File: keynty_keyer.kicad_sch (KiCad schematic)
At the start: 43 parts, among them SW1 Power

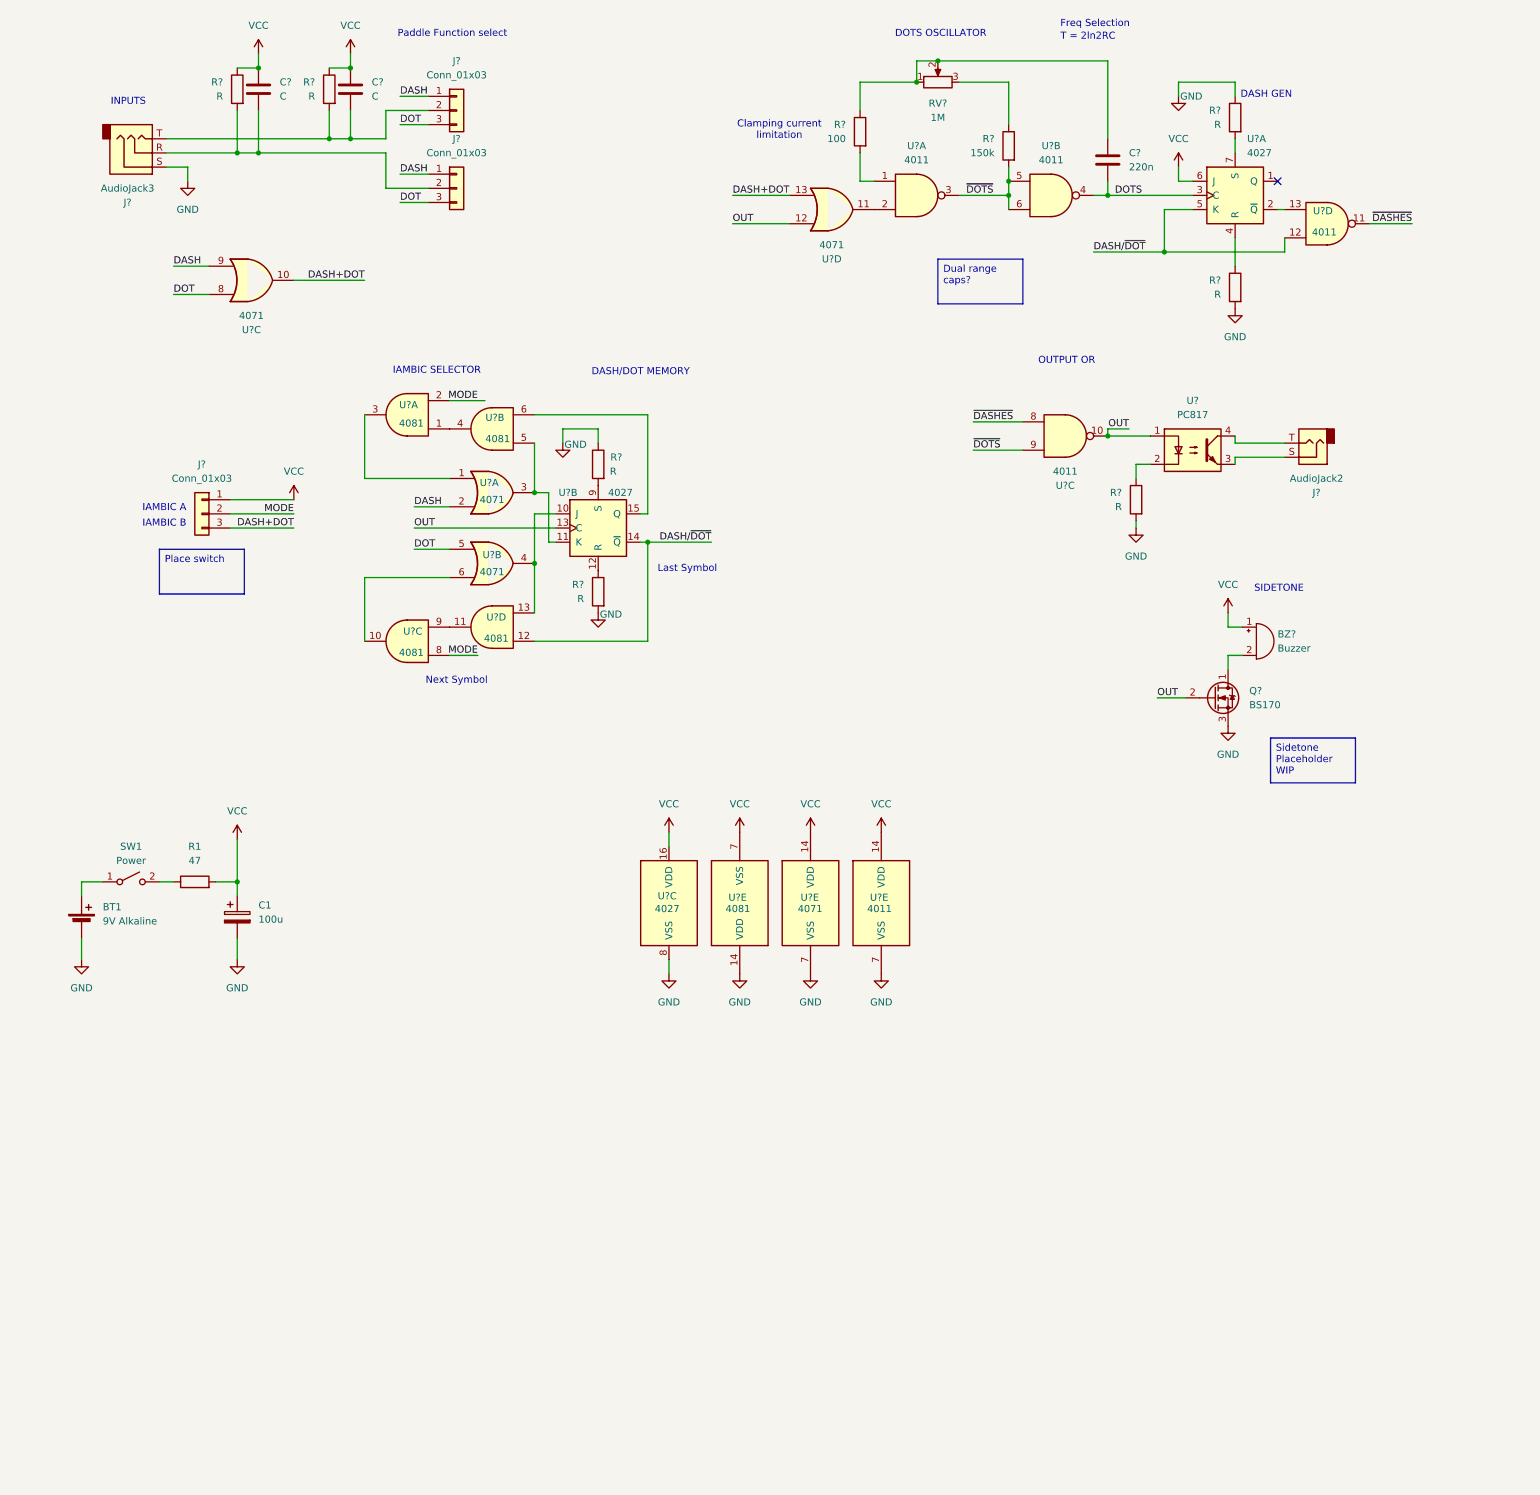
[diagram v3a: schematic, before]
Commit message: added matteo sidetononi e matteo powerleddoni
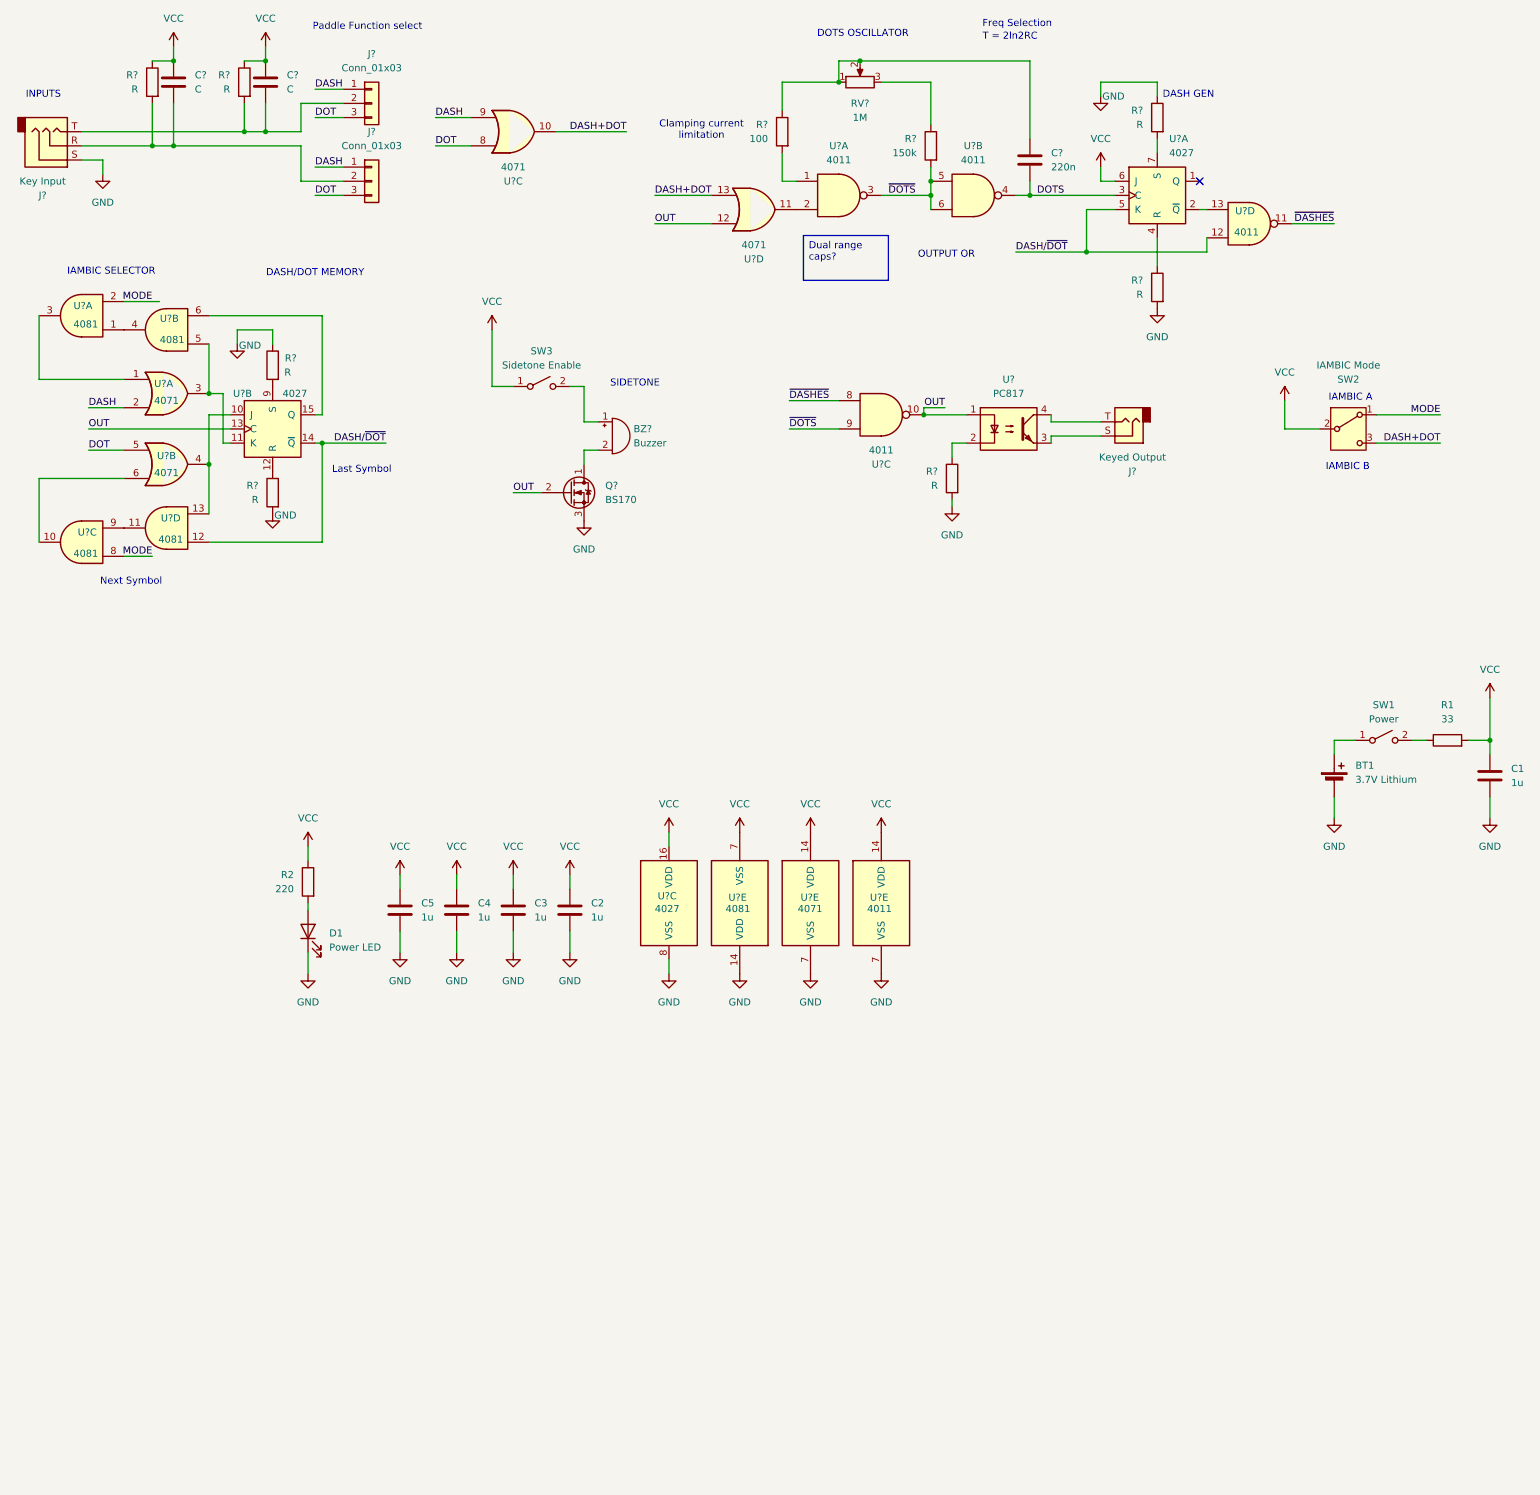
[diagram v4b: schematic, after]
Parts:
- removed C1: 100u, symbol Device:C_Polarized
- removed J?: Conn_01x03, symbol Connector_Generic:Conn_01x03
- added C1, C2, C3, C4, C5: 1u, symbol Device:C
- added D1: Power LED, symbol Device:LED
- added R2: 220, symbol Device:R
- added SW2: IAMBIC Mode, symbol Switch:SW_SPDT
- added SW3: Sidetone Enable, symbol Switch:SW_SPST
- BT1: value 9V Alkaline -> 3.7V Lithium
- J?: value AudioJack3 -> Key Input
- J?: value AudioJack2 -> Keyed Output
- R1: value 47 -> 33
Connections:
- net DASH+DOT: now also SW2.3 (C)
- net GND: now also C1.2, C2.2, C3.2, C4.2, C5.2, D1.1 (K)
- net MODE: now also SW2.1 (A)
- net VCC: now also C1.1, C2.1, C3.1, C4.1, C5.1, R2.1, SW2.2 (B), SW3.1 (A); no longer BZ?.1 (+)
- new net: D1.2 (A), R2.2
- new net: BZ?.1 (+), SW3.2 (B)
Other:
- moved on the sheet: BT1, BZ?, C?, J?, Q?, R1, R?, RV?, SW1, U?, U?A, U?B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

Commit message: corrected IAMBIC selector,added footprints, first PCB Draft
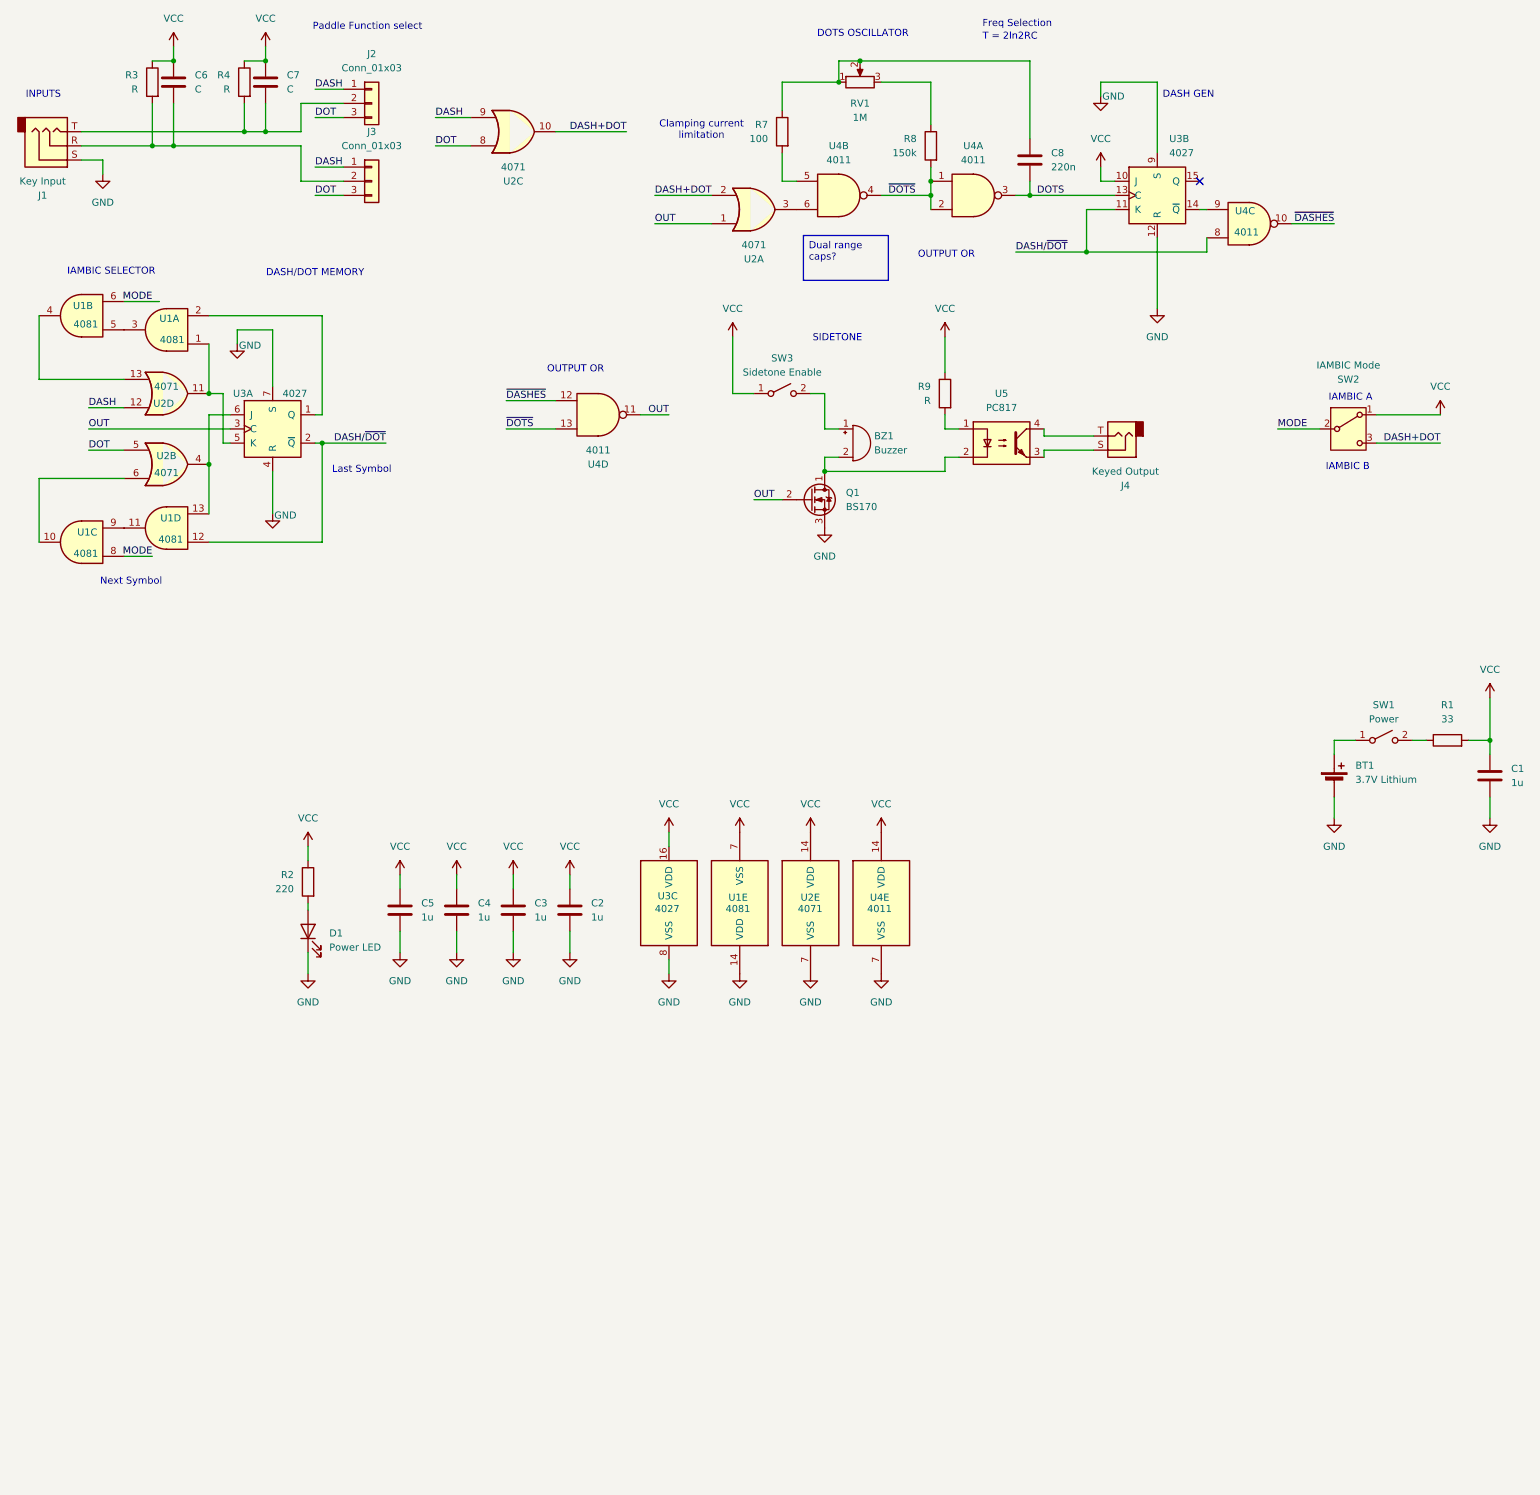
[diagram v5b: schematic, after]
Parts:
- removed R? (x4): R, symbol Device:R
- BT1: footprint (none) -> Battery:BatteryHolder_Keystone_2462_2xAA
- BZ1: renamed from BZ?; footprint (none) -> Buzzer_Beeper:Buzzer_12x9.5RM7.6
- C1, C2, C3, C4, C5: footprint (none) -> Capacitor_SMD:C_0805_2012Metric
- C6, C7, C8: renamed from C?; footprint (none) -> Capacitor_SMD:C_0603_1608Metric
- D1: footprint (none) -> LED_SMD:LED_0603_1608Metric
- J1, J4: renamed from J?; footprint (none) -> Connector_Audio:Jack_3.5mm_CUI_SJ1-3513N_Horizontal
- J2, J3: renamed from J?; footprint (none) -> Connector_PinHeader_2.54mm:PinHeader_1x03_P2.54mm_Vertical
- Q1: renamed from Q?; footprint Package_TO_SOT_THT:TO-92_Inline -> Package_TO_SOT_SMD:SOT-23-3
- R1, R2: footprint (none) -> Resistor_SMD:R_0603_1608Metric
- R3, R4, R7, R8, R9: renamed from R?; footprint (none) -> Resistor_SMD:R_0603_1608Metric
- RV1: renamed from RV?; footprint (none) -> Potentiometer_THT:Potentiometer_Alps_RK09K_Single_Vertical
- SW1, SW2, SW3: footprint (none) -> Button_Switch_THT:SW_Slide_SPDT_Straight_CK_OS102011MS2Q
- U1, U2, U4: renamed from U?; footprint (none) -> Package_SO:SOIC-14_3.9x8.7mm_P1.27mm
- U3: renamed from U?; footprint (none) -> Package_SO:SOIC-16_3.9x9.9mm_P1.27mm
- U5: renamed from U?; footprint Package_DIP:DIP-4_W7.62mm_LongPads -> Package_DIP:DIP-4_W8.89mm_SMDSocket_LongPads
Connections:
- net DASH: now also U2.12; no longer U2.2
- net DASH+DOT: now also U2.2; no longer U2.13
- net DASH/~{DOT}: now also U3.11 (K), U3.2 (~{Q}), U4.8; no longer U3.14 (~{Q}), U3.5 (K), U4.12
- net DOTS: now also U3.13 (C), U4.3; no longer U3.3 (C), U4.4
- net GND: now also U3.12 (R), U3.4 (R), U3.7 (S), U3.9 (S); no longer R9.2
- net MODE: now also SW2.2 (B), U1.6; no longer SW2.1 (A), U1.2
- net OUT: now also U2.1, U3.3 (C), U4.11; no longer U2.12, U3.13 (C), U4.10, U5.1
- net VCC: now also R9.1, SW2.1 (A), U3.10 (J); no longer SW2.2 (B), U3.6 (J)
- net ~{DASHES}: now also U4.10, U4.12; no longer U4.11, U4.8
- net ~{DOTS}: now also U4.1, U4.13, U4.2, U4.4; no longer U4.3, U4.5, U4.6, U4.9
- net at BZ1.2 (-), Q1.1 (D): now also U5.2
- net at U1.13, U2.4: now also U3.6 (J); no longer U3.10 (J)
- net at R7.2: now also U4.5; no longer U4.1
- new net: U3.14 (~{Q}), U4.9
- new net: U1.2, U3.1 (Q)
- new net: U1.1, U2.11, U3.5 (K)
- new net: R9.2, U5.1
- new net: U1.3, U1.5
- new net: U1.4, U2.13
- new net: U2.3, U4.6
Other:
- moved on the sheet: BZ1, J4, Q1, R9, SW3, U4D, U5

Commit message: changed output jack connections, corrected mosfet
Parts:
- removed J4: Keyed Output, Connector_Audio:Jack_3.5mm_CUI_SJ1-3513N_Horizontal, symbol Connector_Audio:AudioJack2
- removed Q1: BS170, Package_TO_SOT_SMD:SOT-23-3, symbol Transistor_FET:BS170
- added J4: Key Input, Connector_Audio:Jack_3.5mm_CUI_SJ1-3513N_Horizontal, symbol Connector_Audio:AudioJack3
- added Q1: ZXM61N02FTC, Package_TO_SOT_SMD:SOT-23, symbol Transistor_FET:BSS138
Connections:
- net GND: now also Q1.2 (S)
- net OUT: now also Q1.1 (G)
- net at BZ1.2 (-), U5.2: now also Q1.3 (D)
- net at U5.3: now also J4.R, J4.S
- net at U5.4: now also J4.T
